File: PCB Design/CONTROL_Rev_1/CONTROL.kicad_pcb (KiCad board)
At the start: 2 copper layers, 40 x 65 mm, 4 parts, among them J1 Conn_01x24_Pin, J2 Conn_01x24_Pin, U1 STM32F446RETx

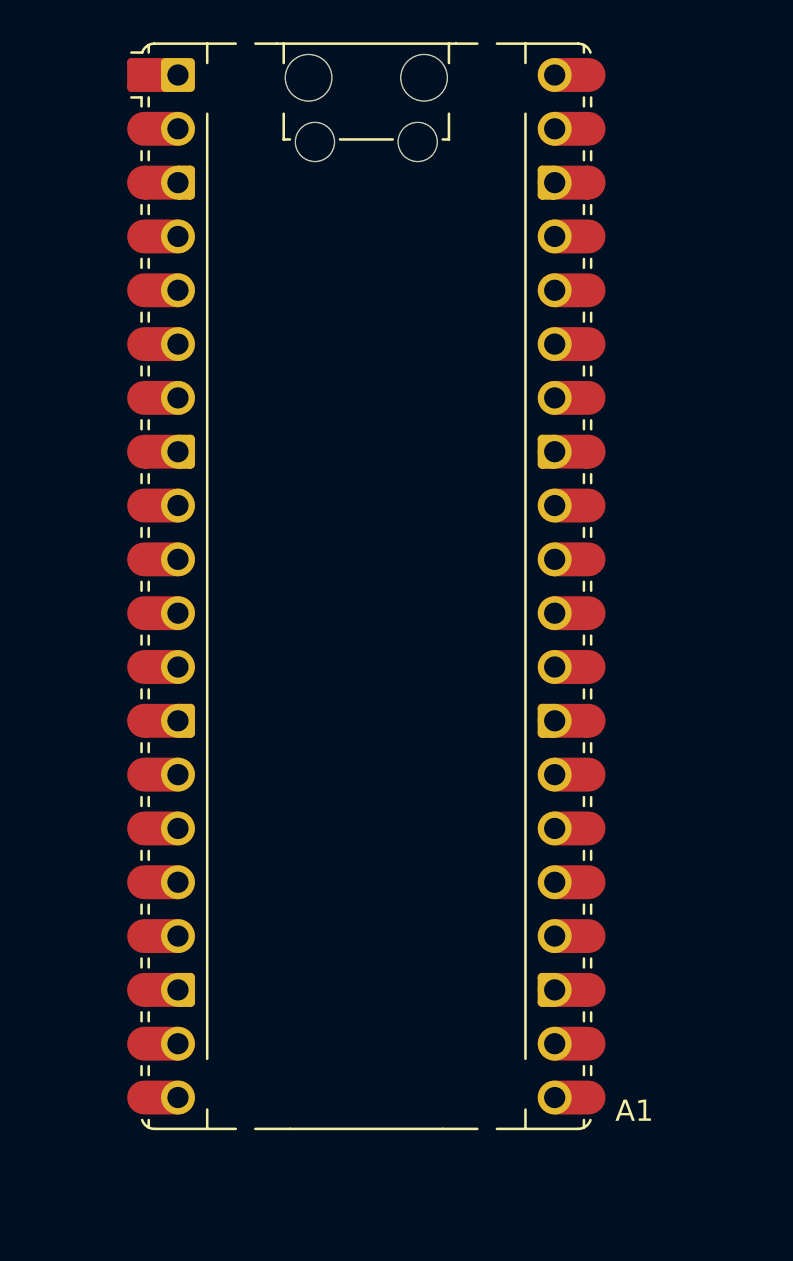
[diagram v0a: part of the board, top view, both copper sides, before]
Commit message: Initial Component Layout of Main MCU
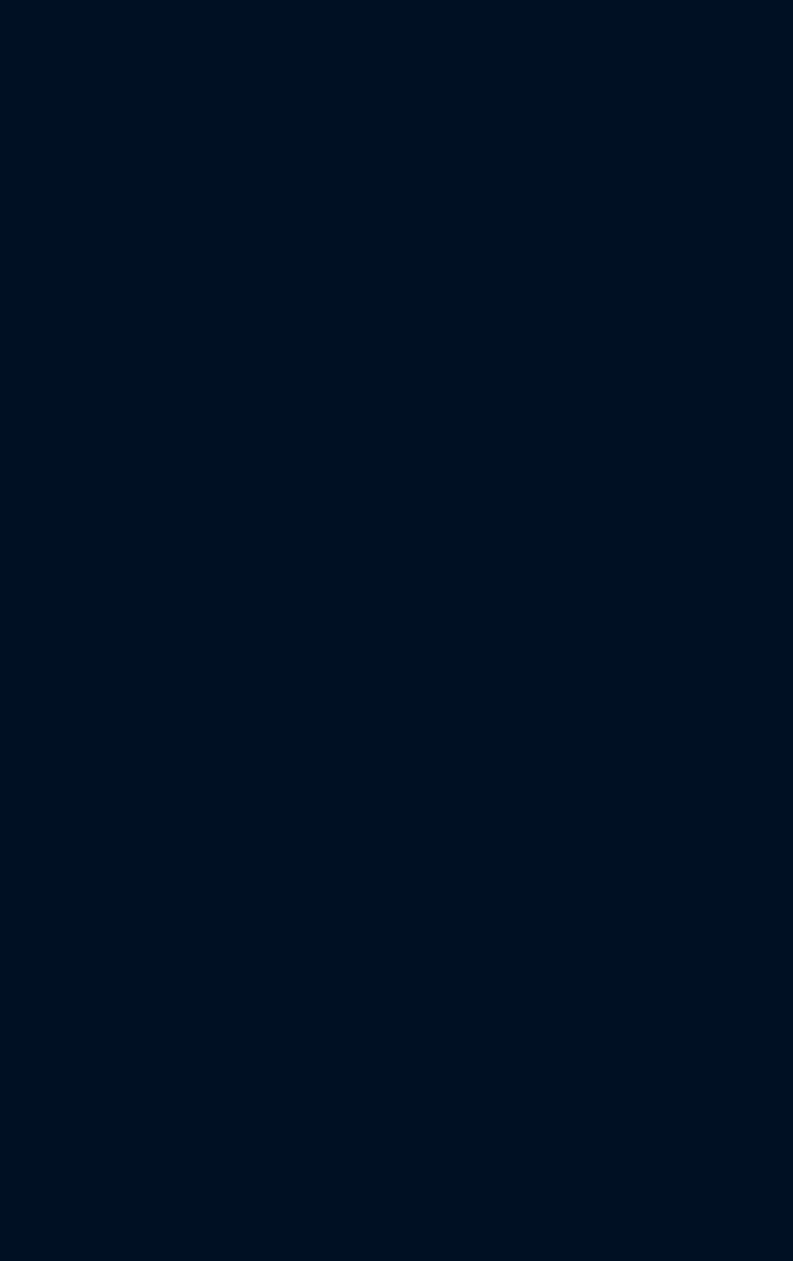
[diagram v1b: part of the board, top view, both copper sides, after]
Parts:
- removed A1: RaspberryPi_Pico, Module:RaspberryPi_Pico_Common_Unspecified

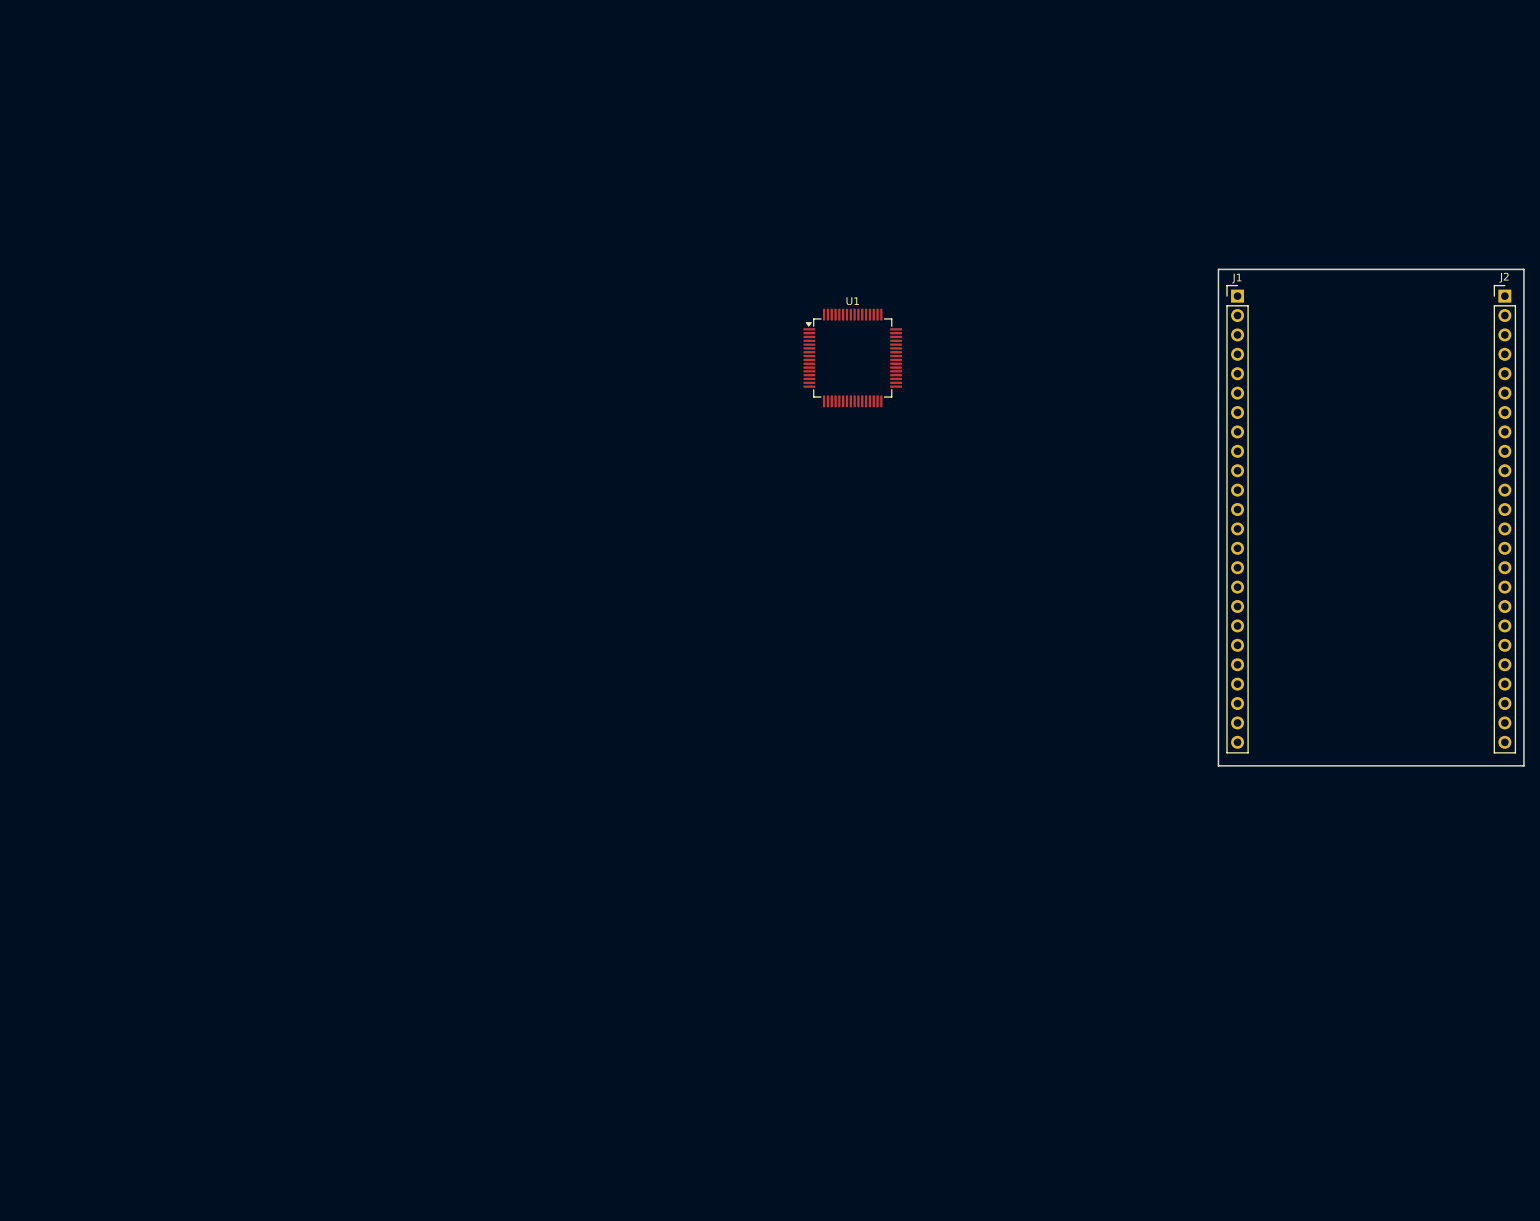
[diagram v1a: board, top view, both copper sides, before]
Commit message: Finished Schematic, Started Placing Components on PCB
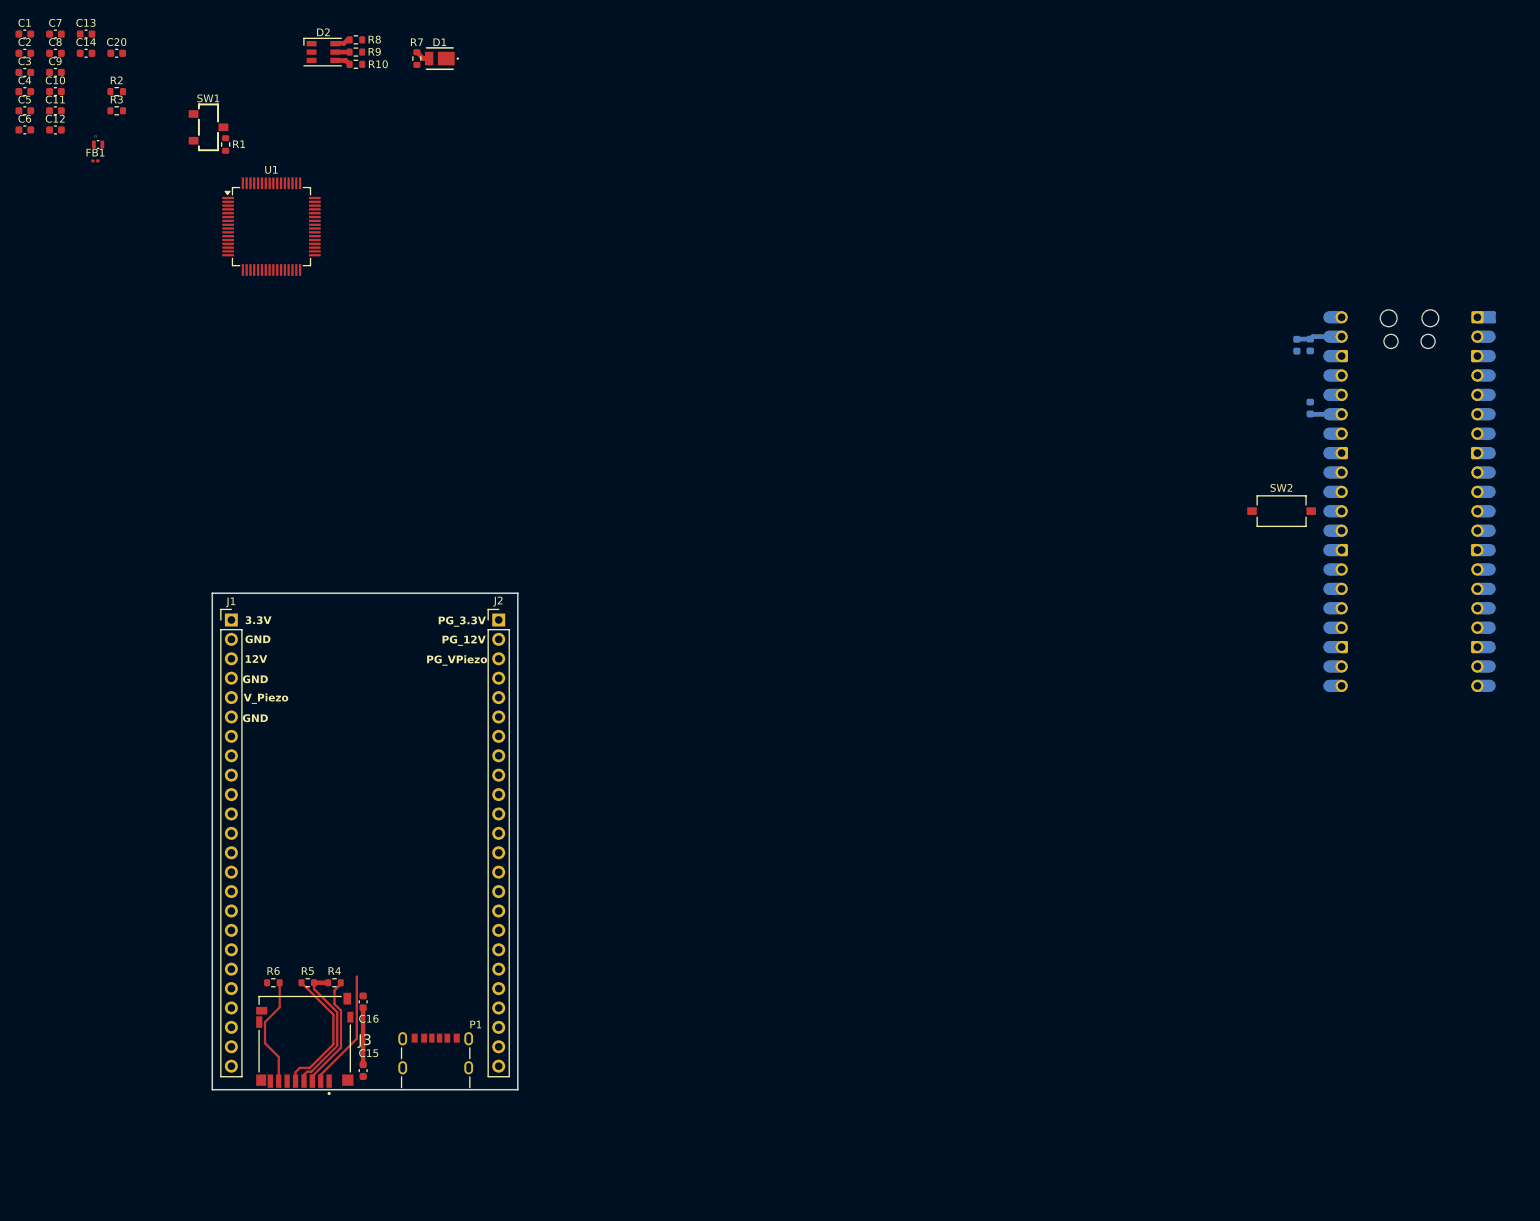
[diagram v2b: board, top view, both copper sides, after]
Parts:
- added A1: RaspberryPi_Pico, Module:RaspberryPi_Pico_Common_Unspecified, B.Cu at (202.0, 88.0)
- added C1: 100n, Capacitor_SMD:C_0603_1608Metric, F.Cu at (20.7, 26.8)
- added C10: 100n, Capacitor_SMD:C_0603_1608Metric, F.Cu at (24.7, 34.3)
- added C11: 10p, Capacitor_SMD:C_0603_1608Metric, F.Cu at (24.7, 36.8)
- added C12: 10p, Capacitor_SMD:C_0603_1608Metric, F.Cu at (24.7, 39.3)
- added C13: 1.2p, Capacitor_SMD:C_0603_1608Metric, F.Cu at (28.7, 26.8)
- added C14: 1.2p, Capacitor_SMD:C_0603_1608Metric, F.Cu at (28.7, 29.3)
- added C15: 0.1u, Capacitor_SMD:C_0603_1608Metric, F.Cu at (65.0, 162.5)
- added C16: 10u, Capacitor_SMD:C_0603_1608Metric, F.Cu at (65.0, 153.5)
- added C17: 100n, Capacitor_SMD:C_0603_1608Metric, B.Cu at (189.0, 75.8)
- added C18: 100n, Capacitor_SMD:C_0603_1608Metric, B.Cu at (189.0, 67.5)
- added C19: 10u, Capacitor_SMD:C_0603_1608Metric, B.Cu at (187.2, 67.5)
- added C2: 100n, Capacitor_SMD:C_0603_1608Metric, F.Cu at (20.7, 29.3)
- added C20: 2.2u, Capacitor_SMD:C_0603_1608Metric, F.Cu at (32.7, 29.3)
- added C3: 100n, Capacitor_SMD:C_0603_1608Metric, F.Cu at (20.7, 31.8)
- added C4: 100n, Capacitor_SMD:C_0603_1608Metric, F.Cu at (20.7, 34.3)
- added C5: 100n, Capacitor_SMD:C_0603_1608Metric, F.Cu at (20.7, 36.8)
- added C6: 10u, Capacitor_SMD:C_0603_1608Metric, F.Cu at (20.7, 39.3)
- added C7: 10n, Capacitor_SMD:C_0603_1608Metric, F.Cu at (24.7, 26.8)
- added C8: 1u, Capacitor_SMD:C_0603_1608Metric, F.Cu at (24.7, 29.3)
- added C9: 1u, Capacitor_SMD:C_0603_1608Metric, F.Cu at (24.7, 31.8)
- added D1: PURPLE, CONTROL:JB2835AWTWU57EA0000N0000001, F.Cu at (75.0, 30.0)
- added D2: LED_RGB, LED_SMD:LED_RGB_PLCC-6, F.Cu at (59.8, 29.1)
- added FB1: 120R, Inductor_SMD:L_0201_0603Metric, F.Cu at (29.9, 43.4)
- added J3: Micro_SD_Card, CONTROL:AMPHENOL_1140084168, F.Cu at (57.4, 163.0)
- added P1: USB_C_Plug_USB2.0, CONTROL:AMPHENOL_10164359-00011LF, F.Cu at (74.5, 161.3)
- added R1: 10k, Resistor_SMD:R_0603_1608Metric, F.Cu at (47.0, 41.2)
- added R10: 1k, Resistor_SMD:R_0603_1608Metric, F.Cu at (64.0, 30.8)
- added R2: 4.7k, Resistor_SMD:R_0603_1608Metric, F.Cu at (32.7, 34.3)
- added R3: 4.7k, Resistor_SMD:R_0603_1608Metric, F.Cu at (32.7, 36.8)
- added R4: 10k, Resistor_SMD:R_0603_1608Metric, F.Cu at (61.2, 151.0)
- added R5: 10k, Resistor_SMD:R_0603_1608Metric, F.Cu at (57.8, 151.0)
- added R6: 10k, Resistor_SMD:R_0603_1608Metric, F.Cu at (53.2, 151.0)
- added R7: 1k, Resistor_SMD:R_0603_1608Metric, F.Cu at (72.0, 30.0)
- added R8: 1k, Resistor_SMD:R_0603_1608Metric, F.Cu at (64.0, 27.6)
- added R9: 1k, Resistor_SMD:R_0603_1608Metric, F.Cu at (64.0, 29.1)
- added SW1: SW_SPDT, CONTROL:B-TYPE, F.Cu at (44.8, 39.0)
- added SW2: SW_Push, Button_Switch_SMD:SW_Tactile_SPST_NO_Straight_CK_PTS636Sx25SMTRLFS, F.Cu at (185.2, 89.2)
- added Y2: 32.768KHz, CONTROL:XTAL_ABS05W-32.768KHZ-D-2-T, F.Cu at (30.3, 41.2)
- U1: value STM32F446RETx -> STM32F446RET6
- moved J1 138.4 mm to (47.8, 103.5)
- moved J2 138.4 mm to (82.8, 103.5)
- moved U1 78.0 mm to (53.0, 52.0)
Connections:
- J1 pad 20: unconnected-(J1-Pin_20-Pad20) -> /TEMP_ALERT
- J1 pad 21: unconnected-(J1-Pin_21-Pad21) -> /ACC_INT1
- J1 pad 22: unconnected-(J1-Pin_22-Pad22) -> /ACC_INT2
- J1 pad 23: unconnected-(J1-Pin_23-Pad23) -> /HI_A
- J1 pad 24: unconnected-(J1-Pin_24-Pad24) -> /LI_A
- J2 pad 20: unconnected-(J2-Pin_20-Pad20) -> /CURRENT_ADC
- J2 pad 21: unconnected-(J2-Pin_21-Pad21) -> /LISTEN_EN
- J2 pad 22: unconnected-(J2-Pin_22-Pad22) -> /ADC_OUT
- J2 pad 23: unconnected-(J2-Pin_23-Pad23) -> /HI_B
- J2 pad 24: unconnected-(J2-Pin_24-Pad24) -> /LI_B
- J2 pad 4: unconnected-(J2-Pin_4-Pad4) -> /SCL
- J2 pad 5: unconnected-(J2-Pin_5-Pad5) -> /SDA
- U1 pad 1: unconnected-(U1-VBAT-Pad1) -> 3.3V
- U1 pad 10: unconnected-(U1-PC2-Pad10) -> /SPI2_MISO
- U1 pad 11: unconnected-(U1-PC3-Pad11) -> /PC3
- U1 pad 12: unconnected-(U1-VSSA-Pad12) -> GND
- U1 pad 13: unconnected-(U1-VDDA-Pad13) -> 3.3VA
- U1 pad 14: unconnected-(U1-PA0-Pad14) -> /ADC1_IN0
- U1 pad 15: unconnected-(U1-PA1-Pad15) -> /ADC1_IN1
- U1 pad 16: unconnected-(U1-PA2-Pad16) -> /ADC1_IN2
- U1 pad 17: unconnected-(U1-PA3-Pad17) -> /ADC1_IN3
- U1 pad 18: Net-(U1-VSS-Pad18) -> GND
- U1 pad 19: unconnected-(U1-VDD-Pad19) -> 3.3V
- U1 pad 2: unconnected-(U1-PC13-Pad2) -> /PC13
- U1 pad 20: unconnected-(U1-PA4-Pad20) -> /HEARTBEAT
- U1 pad 21: unconnected-(U1-PA5-Pad21) -> /SPI_SCK
- U1 pad 22: unconnected-(U1-PA6-Pad22) -> /SPI_MISO
- U1 pad 23: unconnected-(U1-PA7-Pad23) -> /SPI_MOSI
- U1 pad 24: unconnected-(U1-PC4-Pad24) -> /PC4
- U1 pad 25: unconnected-(U1-PC5-Pad25) -> /PC5
- U1 pad 26: unconnected-(U1-PB0-Pad26) -> /PB0
- U1 pad 27: unconnected-(U1-PB1-Pad27) -> /PB1
- U1 pad 28: unconnected-(U1-PB2-Pad28) -> /TIM2_CH4
- U1 pad 29: unconnected-(U1-PB10-Pad29) -> /TIM2_CH3
- U1 pad 3: unconnected-(U1-PC14-Pad3) -> /LSE_IN
- U1 pad 30: unconnected-(U1-VCAP_1-Pad30) -> Net-(U1-VCAP_1)
- U1 pad 31: Net-(U1-VSS-Pad18) -> GND
- U1 pad 32: unconnected-(U1-VDD-Pad32) -> 3.3V
- U1 pad 33: unconnected-(U1-PB12-Pad33) -> /PB12
- U1 pad 34: unconnected-(U1-PB13-Pad34) -> /SPI2_SCK
- U1 pad 35: unconnected-(U1-PB14-Pad35) -> /PB14
- U1 pad 36: unconnected-(U1-PB15-Pad36) -> /PB15
- U1 pad 37: unconnected-(U1-PC6-Pad37) -> /PC6
- U1 pad 38: unconnected-(U1-PC7-Pad38) -> /PC7
- U1 pad 39: unconnected-(U1-PC8-Pad39) -> /PC8
- U1 pad 4: unconnected-(U1-PC15-Pad4) -> /LSE_OUT
- U1 pad 40: unconnected-(U1-PC9-Pad40) -> /PC9
- U1 pad 41: unconnected-(U1-PA8-Pad41) -> /CS
- U1 pad 42: unconnected-(U1-PA9-Pad42) -> /PA9
- U1 pad 43: unconnected-(U1-PA10-Pad43) -> /PA10
- U1 pad 44: unconnected-(U1-PA11-Pad44) -> /USB_D-
- U1 pad 45: unconnected-(U1-PA12-Pad45) -> /USB_D+
- U1 pad 46: unconnected-(U1-PA13-Pad46) -> /SWDIO
- U1 pad 47: Net-(U1-VSS-Pad18) -> GND
- U1 pad 48: unconnected-(U1-VDD-Pad48) -> 3.3V
- U1 pad 49: unconnected-(U1-PA14-Pad49) -> /SWCLK
- U1 pad 5: unconnected-(U1-PH0-Pad5) -> /HSE_IN
- U1 pad 50: unconnected-(U1-PA15-Pad50) -> /TIM2_CH1
- U1 pad 51: unconnected-(U1-PC10-Pad51) -> /UART_TX
- U1 pad 52: unconnected-(U1-PC11-Pad52) -> /UART_RX
- U1 pad 53: unconnected-(U1-PC12-Pad53) -> /PC12
- U1 pad 54: unconnected-(U1-PD2-Pad54) -> /PD2
- U1 pad 55: unconnected-(U1-PB3-Pad55) -> /SWO
- U1 pad 56: unconnected-(U1-PB4-Pad56) -> /PB4
- U1 pad 57: unconnected-(U1-PB5-Pad57) -> /PB5
- U1 pad 58: unconnected-(U1-PB6-Pad58) -> /PB6
- U1 pad 59: unconnected-(U1-PB7-Pad59) -> /SDA
- U1 pad 6: unconnected-(U1-PH1-Pad6) -> /HSE_OUT
- U1 pad 60: unconnected-(U1-BOOT0-Pad60) -> /BOOT0
- U1 pad 61: unconnected-(U1-PB8-Pad61) -> /SCL
- U1 pad 62: unconnected-(U1-PB9-Pad62) -> /TIM2_CH2
- U1 pad 63: Net-(U1-VSS-Pad18) -> GND
- U1 pad 64: unconnected-(U1-VDD-Pad64) -> 3.3V
- U1 pad 7: unconnected-(U1-NRST-Pad7) -> /NRST
- U1 pad 8: unconnected-(U1-PC0-Pad8) -> /PC0
- U1 pad 9: unconnected-(U1-PC1-Pad9) -> /SPI2_MOSI
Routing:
- net 3.3V: track 0.00 -> 35.7 mm
- net /SPI2_SCK: track 0.00 -> 17.4 mm
- net /CS: track 0.00 -> 15.7 mm
- net /SPI2_MOSI: track 0.00 -> 15.1 mm
- net /SPI2_MISO: track 0.00 -> 14.4 mm
- net Net-(D2-RA): track 0.00 -> 2.08 mm
- net Net-(D2-BA): track 0.00 -> 2.08 mm
- net Net-(D1-A): track 0.00 -> 1.95 mm
- net Net-(D2-GA): track 0.00 -> 1.88 mm

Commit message: Minor Schematic Updates and PCB Routing
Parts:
- removed SW2: SW_Push, Button_Switch_SMD:SW_Tactile_SPST_NO_Straight_CK_PTS636Sx25SMTRLFS
- added Y1: 16MHz, Crystal:Crystal_SMD_3225-4Pin_3.2x2.5mm, F.Cu at (69.3, 144.1)
- A1: footprint Module:RaspberryPi_Pico_Common_Unspecified -> Module:RaspberryPi_Pico_Common_THT; moved to F.Cu
- C10, C20: moved to B.Cu
- P1: footprint CONTROL:AMPHENOL_10164359-00011LF -> Connector_USB:USB_C_Receptacle_GCT_USB4085
- moved A1 144.9 mm to (57.8, 101.8), turned to 0 degrees
- moved C4 143.9 mm to (70.9, 169.2), turned to 180 degrees
- moved R8 140.5 mm to (77.4, 167.4), turned to 180 degrees
- moved SW1 139.5 mm to (67.8, 176.6), turned to 0 degrees
- moved C3 139.4 mm to (59.7, 165.7), turned to 90 degrees
- moved D2 138.4 mm to (81.7, 165.8), turned to 180 degrees
- moved C20 138.0 mm to (63.5, 163.8), turned to 90 degrees
- moved C1 137.9 mm to (73.3, 154.3)
- moved R9 137.3 mm to (77.4, 165.8), turned to 180 degrees
- moved C2 135.1 mm to (59.9, 158.6), turned to 90 degrees
- moved R1 135.0 mm to (70.0, 174.3), turned to 0 degrees
- moved R10 134.1 mm to (77.4, 164.2), turned to 180 degrees
- moved C7 133.2 mm to (65.4, 153.6)
- moved C5 132.9 mm to (75.0, 158.1), turned to -90 degrees
- moved C13 131.9 mm to (71.7, 151.6)
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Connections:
- A1 pad 30: Net-(A1-RUN) -> unconnected-(A1-RUN-Pad30)
- J1 pad 15: unconnected-(J1-Pin_15-Pad15) -> /ADC1_IN0
- J1 pad 16: unconnected-(J1-Pin_16-Pad16) -> /ADC1_IN2
- J1 pad 17: unconnected-(J1-Pin_17-Pad17) -> /ADC1_IN1
- J1 pad 18: unconnected-(J1-Pin_18-Pad18) -> /ADC1_IN3
- J1 pad 19: unconnected-(J1-Pin_19-Pad19) -> /PC4
- J1 pad 20: /TEMP_ALERT -> /PC5
- J1 pad 21: /ACC_INT1 -> /PB0
- J1 pad 22: /ACC_INT2 -> /PB1
- J2 pad 1: /PG_3.3V -> /PC3
- J2 pad 15: unconnected-(J2-Pin_15-Pad15) -> /PC8
- J2 pad 16: unconnected-(J2-Pin_16-Pad16) -> /PC9
- J2 pad 17: unconnected-(J2-Pin_17-Pad17) -> /PA9
- J2 pad 18: unconnected-(J2-Pin_18-Pad18) -> /PA10
- J2 pad 19: unconnected-(J2-Pin_19-Pad19) -> /SCL
- J2 pad 2: /PG_12V -> /PC0
- J2 pad 20: /CURRENT_ADC -> /SDA
- J2 pad 21: /LISTEN_EN -> /PB6
- J2 pad 22: /ADC_OUT -> /LISTEN_EN
- J2 pad 3: /PG_VPiezo -> /PC13
- J2 pad 4: /SCL -> unconnected-(J2-Pin_4-Pad4)
- J2 pad 5: /SDA -> unconnected-(J2-Pin_5-Pad5)
- U1 pad 28: /TIM2_CH4 -> /HI_A
- U1 pad 29: /TIM2_CH3 -> /LI_A
- U1 pad 50: /TIM2_CH1 -> /LI_B
- U1 pad 53: /PC12 -> /LED_RED
- U1 pad 54: /PD2 -> /LED_GREEN
- U1 pad 56: /PB4 -> /LED_BLUE
- U1 pad 57: /PB5 -> /LISTEN_EN
- U1 pad 62: /TIM2_CH2 -> /HI_B
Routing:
- net /UART_TX: track 0.00 -> 71.0 mm, vias 0 -> 1
- net /UART_RX: track 0.00 -> 68.6 mm, vias 0 -> 1
- net /PC3: track 0.00 -> 63.2 mm, vias 0 -> 1
- net /PC0: track 0.00 -> 59.8 mm, vias 0 -> 1
- net /SPI_SCK: track 0.00 -> 56.3 mm, vias 0 -> 1
- net /SPI_MOSI: track 0.00 -> 55.9 mm, vias 0 -> 1
- net /PC13: track 0.00 -> 54.6 mm, vias 0 -> 1
- net /SPI_MISO: track 0.00 -> 51.9 mm, vias 0 -> 1
- net /HEARTBEAT: track 0.00 -> 50.5 mm
- net /PC8: track 0.00 -> 36.4 mm, vias 0 -> 1
- net (no net): track 0.00 -> 34.3 mm, vias 0 -> 25
- net /PC9: track 0.00 -> 33.4 mm, vias 0 -> 1
- net /PA9: track 0.00 -> 30.3 mm, vias 0 -> 1
- net /PA10: track 0.00 -> 27.8 mm, vias 0 -> 1
- net /ADC1_IN0: track 0.00 -> 27.6 mm, vias 0 -> 1
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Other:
- board size 40 x 65 mm -> 40 x 80 mm
